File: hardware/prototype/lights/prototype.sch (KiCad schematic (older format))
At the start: 68 parts, among them CON1 BARREL_JACK, P1 CONN_01X06, U1 MAX7221

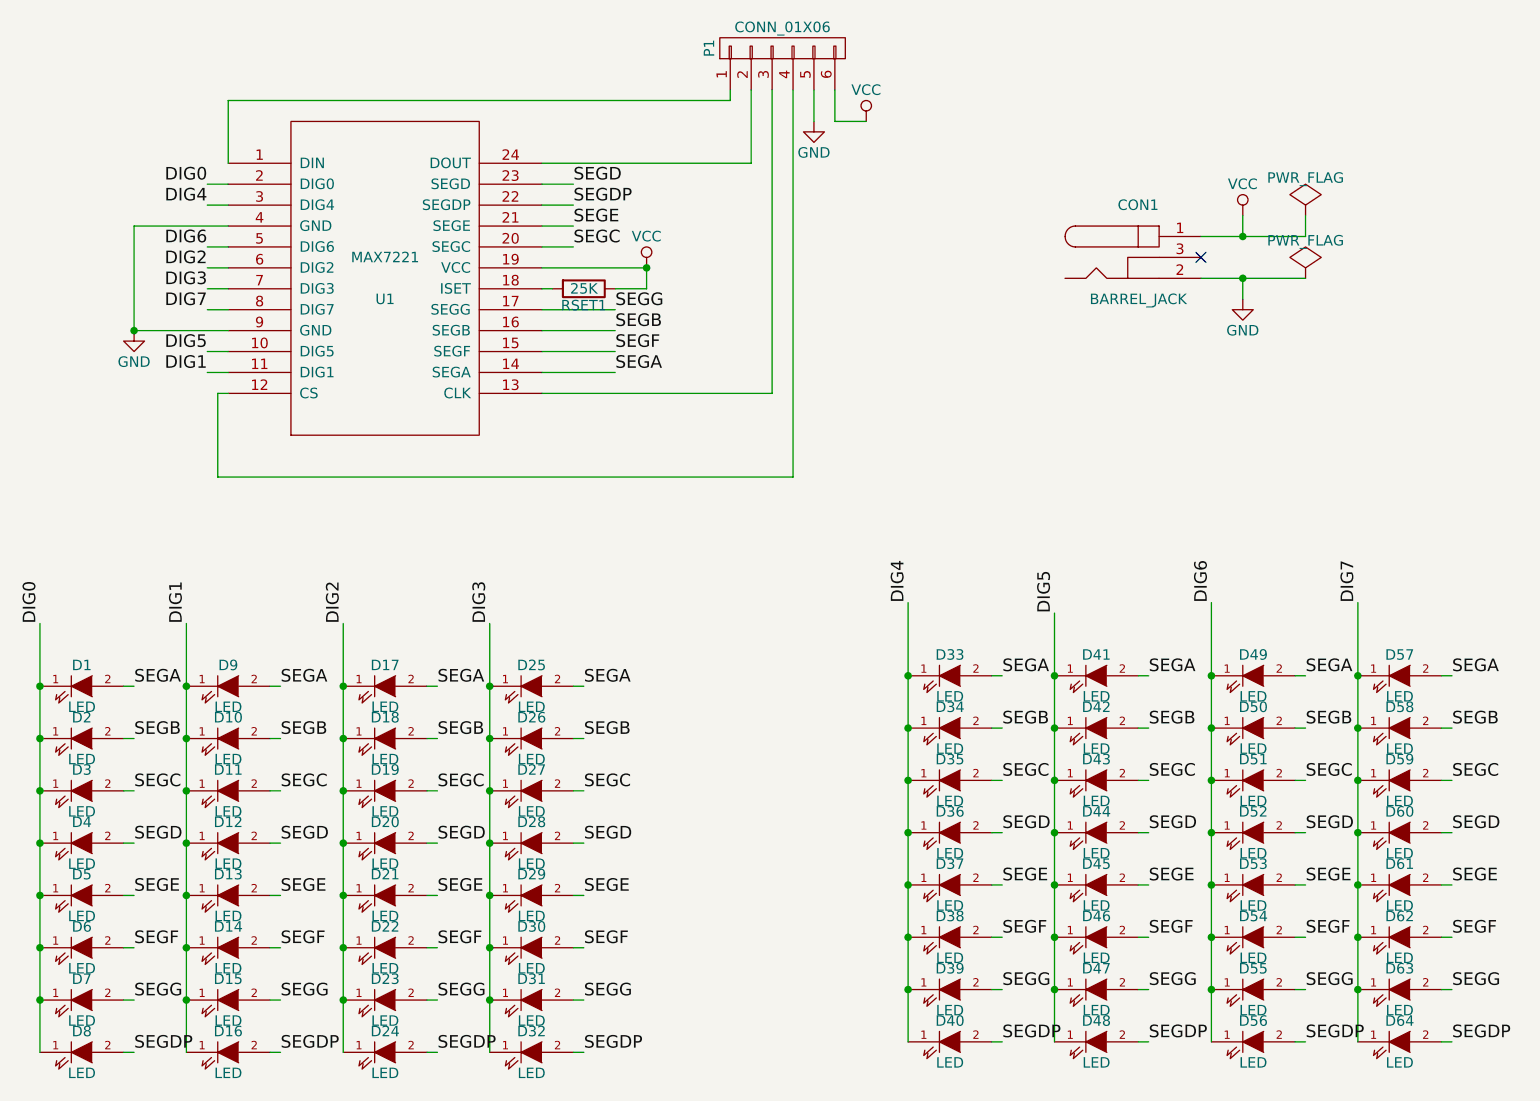
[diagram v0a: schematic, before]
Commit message: Move prototype circuit schematic into subfolder as it only includes the LED matrix circuit.
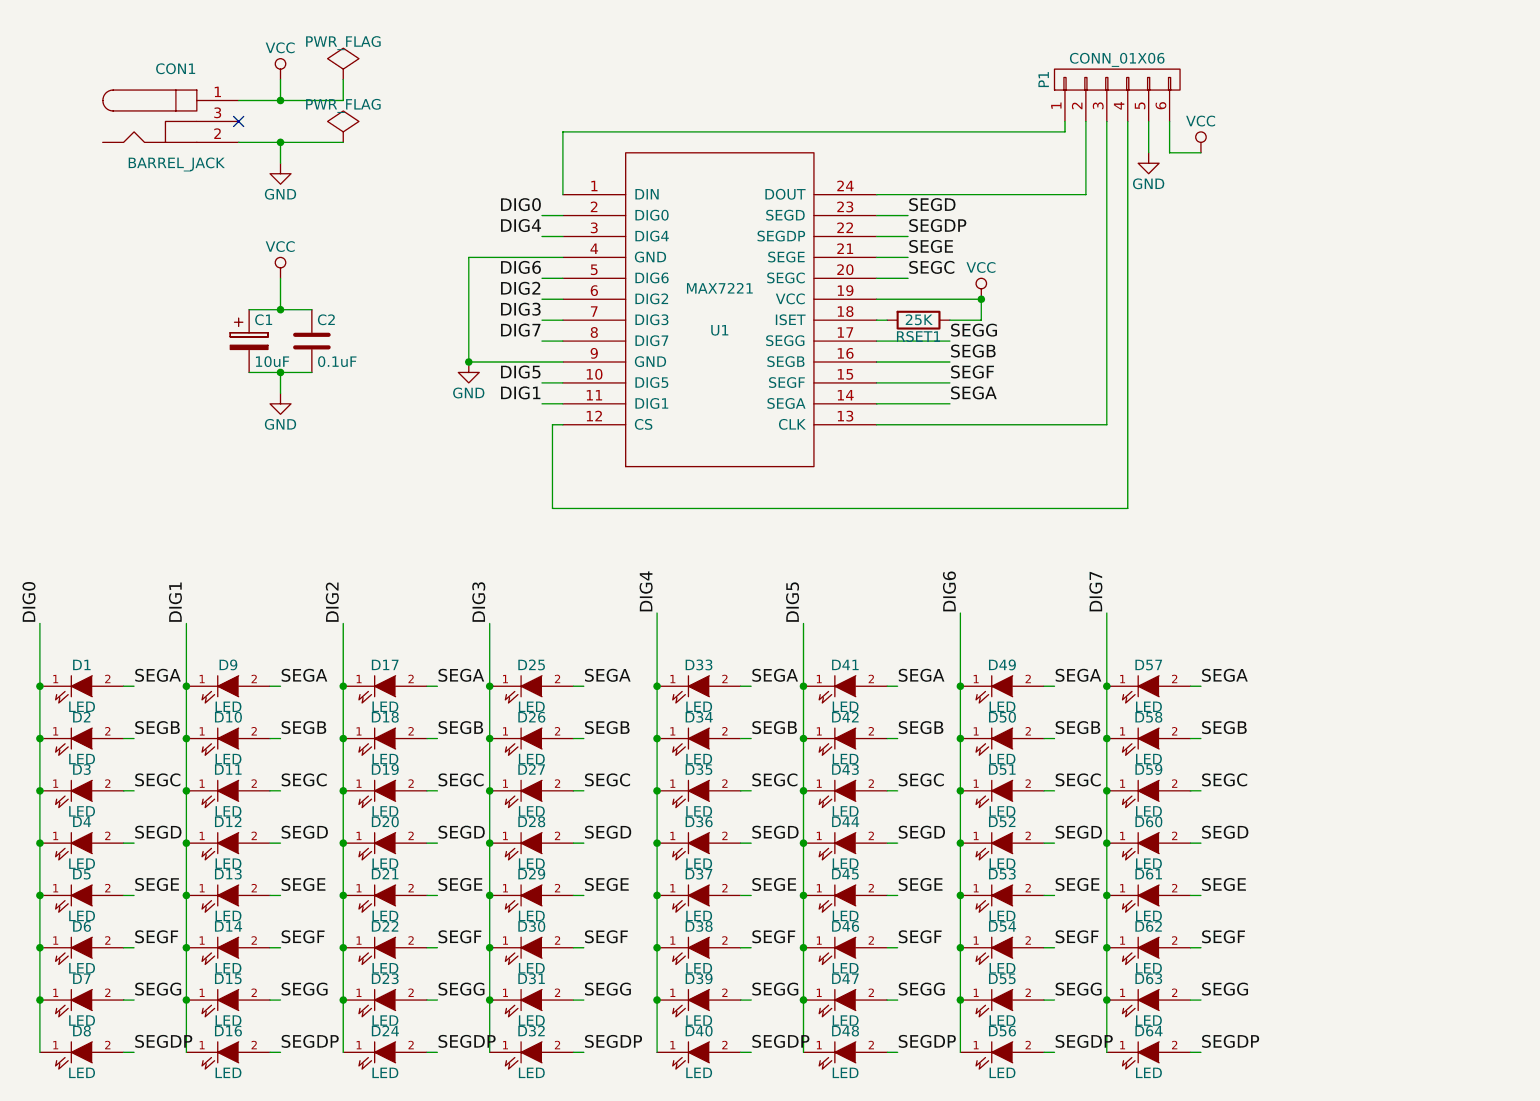
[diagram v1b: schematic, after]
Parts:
- added C1: 10uF, symbol CP
- added C2: 0.1uF, symbol C
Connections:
- net GND: now also C1.2, C2.2
- net VCC: now also C1.1, C2.1
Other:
- moved on the sheet: CON1, D33, D34, D35, D36, D37, D38, D39, D40, D41, D42, D43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
